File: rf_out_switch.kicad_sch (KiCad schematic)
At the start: 10 parts, among them P15 CONUFL001-SMD-T, P16 CONUFL001-SMD-T, U33 QPC1022TR7, U34 QPC1022TR7

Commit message: Work on cleaning up all values for things
Signed-off-by: Corey Minyard <corey@minyard.net>
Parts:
- R104, R109: value 50R >=2W -> 50Ω >=2W
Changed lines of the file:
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@@
 			)
 		)
-		(property "Value" "50R >=2W"
+		(property "Value" "50Ω >=2W"
 			(at 78.74 76.708 90)
 			(effects
@@
 			)
 		)
-		(property "Value" "50R >=2W"
+		(property "Value" "50Ω >=2W"
 			(at 195.834 110.998 90)
 			(effects

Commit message: Lots of updates to ease manufacturing
Component changes, changes in the formatting of the values, etc.

Signed-off-by: Corey Minyard <corey@minyard.net>
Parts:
- L39: value 470n -> 470nH
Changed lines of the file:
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@@
 			)
 		)
-		(property "Value" "470n"
+		(property "Value" "470nH"
 			(at 97.282 53.848 90)
 			(effects

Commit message: Update all resistors to have an ohm symbol
Make it more clean in the BOM what they are.

Signed-off-by: Corey Minyard <corey@minyard.net>
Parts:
- R105, R106: value 10K -> 10KΩ
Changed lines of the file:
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@@
 			)
 		)
-		(property "Value" "10K"
+		(property "Value" "10KΩ"
 			(at 86.868 140.843 0)
 			(effects
@@
 			)
 		)
-		(property "Value" "10K"
+		(property "Value" "10KΩ"
 			(at 86.868 130.683 0)
 			(effects

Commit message: Massive rework of filtering and inductors
Now that I know how inductors really work.

Signed-off-by: Corey Minyard <corey@minyard.net>
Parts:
- R107: now not fitted
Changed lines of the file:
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@@
 		(in_bom yes)
 		(on_board yes)
-		(dnp no)
+		(dnp yes)
 		(property "Reference" "R107"
 			(at 132.588 87.7316 0)

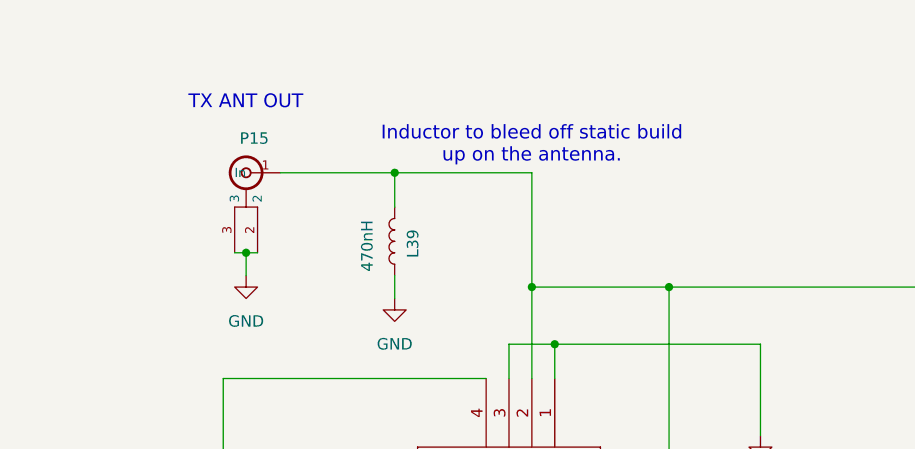
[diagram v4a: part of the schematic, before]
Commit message: More cleanups on the filtering
Signed-off-by: Corey Minyard <corey@minyard.net>
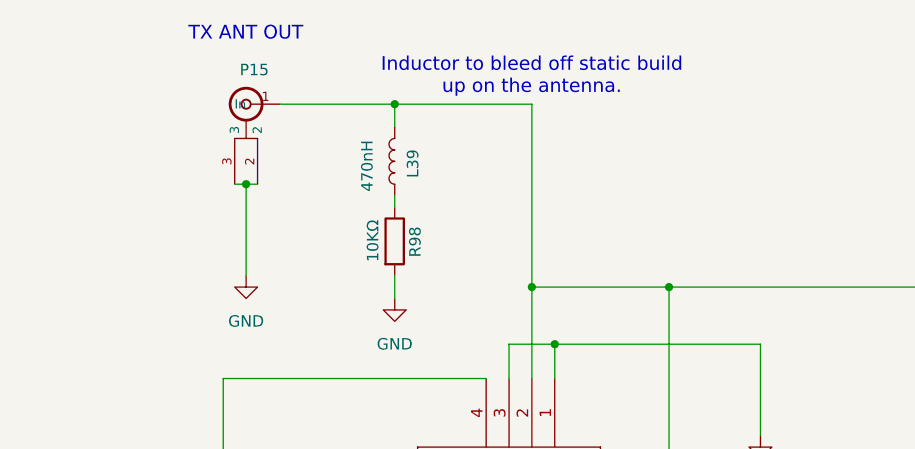
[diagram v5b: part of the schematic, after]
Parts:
- added R98: 10KΩ, Resistor_SMD:R_0402_1005Metric_Pad0.72x0.64mm_HandSolder, symbol Device:R
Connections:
- net GND: now also R98.2; no longer L39.2
- new net: L39.2, R98.1
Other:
- moved on the sheet: L39, P15
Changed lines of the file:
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@@
 	(text "TX ANT OUT"
 		(exclude_from_sim no)
-		(at 90.17 38.862 0)
+		(at 90.17 31.242 0)
 		(effects
 			(font
@@
 	(text "Inductor to bleed off static build\nup on the antenna."
 		(exclude_from_sim no)
-		(at 115.57 42.672 0)
+		(at 115.57 35.052 0)
 		(effects
 			(font
@@
 	)
 	(junction
-		(at 100.33 45.72)
-		(diameter 0)
-		(color 0 0 0 0)
-	)
-	(junction
-		(at 83.82 54.61)
+		(at 100.33 38.1)
 		(diameter 0)
 		(color 0 0 0 0)
@@
 	)
 	(junction
+		(at 83.82 46.99)
+		(diameter 0)
+		(color 0 0 0 0)
+	)
+	(junction
 		(at 115.57 58.42)
 		(diameter 0)
@@
 	(wire
 		(pts
-			(xy 100.33 45.72) (xy 115.57 45.72)
-		)
-		(stroke
-			(width 0)
-			(type default)
-		)
-	)
-	(wire
-		(pts
 			(xy 130.81 58.42) (xy 187.96 58.42)
 		)
@@
 	(wire
 		(pts
+			(xy 100.33 57.15) (xy 100.33 59.69)
+		)
+		(stroke
+			(width 0)
+			(type default)
+		)
+	)
+	(wire
+		(pts
 			(xy 172.72 46.99) (xy 172.72 49.53)
 		)
@@
 	(wire
 		(pts
-			(xy 87.63 45.72) (xy 100.33 45.72)
+			(xy 87.63 38.1) (xy 100.33 38.1)
 		)
 		(stroke
@@
 	(wire
 		(pts
-			(xy 83.82 54.61) (xy 85.09 54.61)
-		)
-		(stroke
-			(width 0)
-			(type default)
-		)
-	)
-	(wire
-		(pts
-			(xy 83.82 54.61) (xy 83.82 57.15)
+			(xy 100.33 48.26) (xy 100.33 49.53)
+		)
+		(stroke
+			(width 0)
+			(type default)
+		)
+	)
+	(wire
+		(pts
+			(xy 83.82 46.99) (xy 85.09 46.99)
+		)
+		(stroke
+			(width 0)
+			(type default)
+		)
+	)
+	(wire
+		(pts
+			(xy 83.82 46.99) (xy 83.82 57.15)
 		)
 		(stroke
@@
 	(wire
 		(pts
-			(xy 83.82 54.61) (xy 82.55 54.61)
+			(xy 83.82 46.99) (xy 82.55 46.99)
 		)
 		(stroke
@@
 	(wire
 		(pts
-			(xy 115.57 45.72) (xy 115.57 58.42)
+			(xy 115.57 38.1) (xy 115.57 58.42)
 		)
 		(stroke
@@
 	(wire
 		(pts
-			(xy 100.33 57.15) (xy 100.33 59.69)
-		)
-		(stroke
-			(width 0)
-			(type default)
-		)
-	)
-	(wire
-		(pts
 			(xy 81.28 68.58) (xy 110.49 68.58)
 		)
@@
 	(wire
 		(pts
+			(xy 100.33 38.1) (xy 115.57 38.1)
+		)
+		(stroke
+			(width 0)
+			(type default)
+		)
+	)
+	(wire
+		(pts
 			(xy 172.72 46.99) (xy 171.45 46.99)
 		)
@@
 	(wire
 		(pts
+			(xy 100.33 38.1) (xy 100.33 40.64)
+		)
+		(stroke
+			(width 0)
+			(type default)
+		)
+	)
+	(wire
+		(pts
 			(xy 190.5 99.06) (xy 190.5 118.11)
 		)
@@
 		(pts
 			(xy 193.04 125.73) (xy 207.01 125.73)
-		)
-		(stroke
-			(width 0)
-			(type default)
-		)
-	)
-	(wire
-		(pts
-			(xy 100.33 45.72) (xy 100.33 49.53)
 		)
 		(stroke
@@
 	(symbol
 		(lib_id "Device:L")
-		(at 100.33 53.34 0)
+		(at 100.33 44.45 0)
 		(mirror y)
 		(unit 1)
@@
 		(dnp no)
 		(property "Reference" "L39"
-			(at 102.362 53.594 90)
+			(at 102.362 44.704 90)
 			(effects
 				(font
@@
 		)
 		(property "Value" "470nH"
-			(at 97.282 53.848 90)
+			(at 97.282 44.958 90)
 			(effects
 				(font
@@
 		)
 		(property "Footprint" "Inductor_SMD:L_0805_2012Metric_Pad1.05x1.20mm_HandSolder"
-			(at 100.33 53.34 0)
+			(at 100.33 44.45 0)
 			(effects
 				(font
@@
 		)
 		(property "Datasheet" "~"
-			(at 100.33 53.34 0)
+			(at 100.33 44.45 0)
 			(effects
 				(font
@@
 		)
 		(property "Description" ""
-			(at 100.33 53.34 0)
+			(at 100.33 44.45 0)
 			(effects
 				(font
@@
 	)
 	(symbol
+		(lib_id "Device:R")
+		(at 100.33 53.34 0)
+		(unit 1)
+		(exclude_from_sim no)
+		(in_bom yes)
+		(on_board yes)
+		(dnp no)
+		(property "Reference" "R98"
+			(at 102.616 55.118 90)
+			(effects
+				(font
+					(size 1.27 1.27)
+				)
+				(justify left)
+			)
+		)
+		(property "Value" "10KΩ"
+			(at 97.917 55.626 90)
+			(effects
+				(font
+					(size 1.27 1.27)
+				)
+				(justify left)
+			)
+		)
+		(property "Footprint" "Resistor_SMD:R_0402_1005Metric_Pad0.72x0.64mm_HandSolder"
+			(at 98.552 53.34 90)
+			(effects
+				(font
+					(size 1.27 1.27)
+				)
+				(hide yes)
+			)
+		)
+		(property "Datasheet" "~"
+			(at 100.33 53.34 0)
+			(effects
+				(font
+					(size 1.27 1.27)
+				)
+			)
+		)
+		(property "Description" ""
+			(at 100.33 53.34 0)
+			(effects
+				(font
+					(size 1.27 1.27)
+				)
+			)
+		)
+		(pin "1"
+		)
+		(pin "2"
+		)
+		(instances
+			(project "PacSat_AFSK"
+				(path "/cc9f42d2-6985-41ac-acab-5ab7b01c5b38/4fa888af-703c-49ed-93bb-d56d2f02c470/26e0c845-9451-4c79-aef3-943c70af8ca9"
+					(reference "R98")
+					(unit 1)
+				)
+			)
+		)
+	)
+	(symbol
 		(lib_id "power:GND")
 		(at 207.01 72.39 0)
@@
 	(symbol
 		(lib_id "PACSAT_DEV_misc:U_FL")
-		(at 83.82 45.72 0)
+		(at 83.82 38.1 0)
 		(mirror y)
 		(unit 1)
@@
 		(dnp no)
 		(property "Reference" "P15"
-			(at 86.36 41.91 0)
+			(at 86.36 34.29 0)
 			(effects
 				(font
@@
 		)
 		(property "Value" "CONUFL001-SMD-T"
-			(at 83.82 45.72 0)
+			(at 83.82 38.1 0)
 			(effects
 				(font
@@
 		)
 		(property "Footprint" "PacSatDev_misc:CONN1_CONUFL_TEC"
-			(at 83.82 45.72 0)
+			(at 83.82 38.1 0)
 			(effects
 				(font
@@
 		)
 		(property "Datasheet" ""
-			(at 83.82 45.72 0)
+			(at 83.82 38.1 0)
 			(effects
 				(font
@@
 		)
 		(property "Description" ""
-			(at 83.82 45.72 0)
-			(effects
-				(font
+			(at 83.82 38.1 0)
+			(effects
+				(font

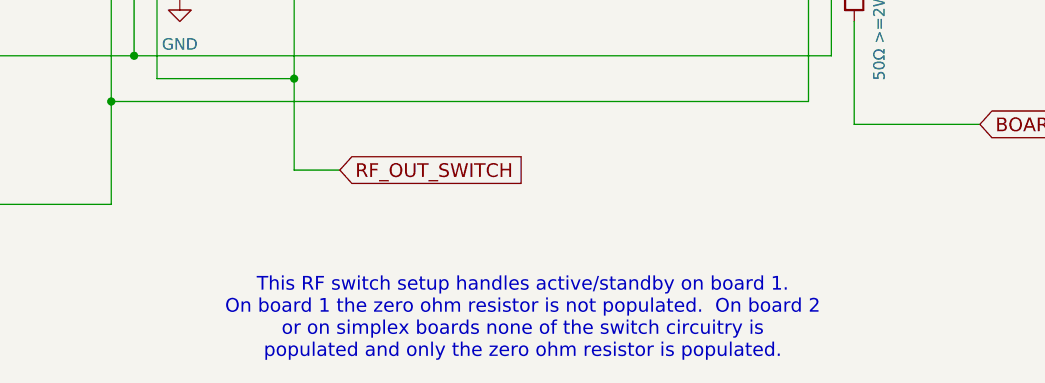
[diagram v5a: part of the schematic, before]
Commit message: Track and doc cleanups
Signed-off-by: Corey Minyard <corey@minyard.net>
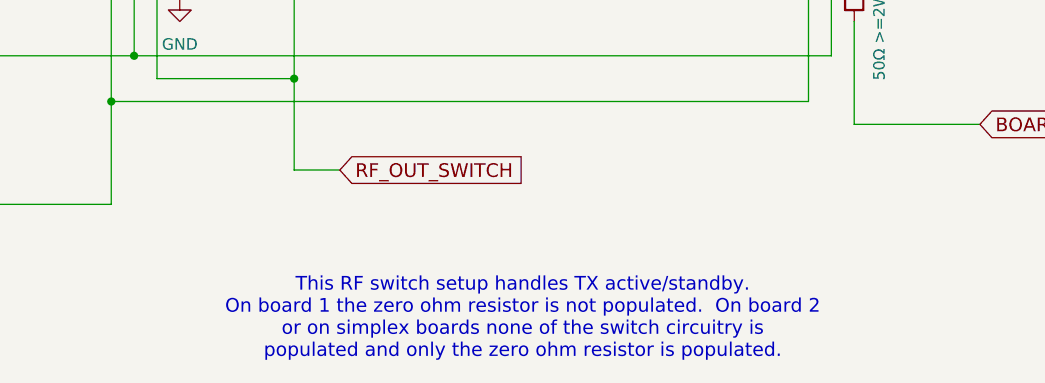
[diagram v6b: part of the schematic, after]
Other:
- note added: "This RF switch setup handles TX active/standby. On board 1 the zero ohm resistor is not populated. On board 2 or on simplex boards none of the switch circuitry is populated and only the zero ohm resistor is populated."
- note removed: "This RF switch setup handles active/standby on board 1. On board 1 the zero ohm resistor is not populated. On board 2 or on simplex boards none of the switch circuitry is populated and only the zero ohm resistor is populated."
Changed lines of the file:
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@@
 		)
 	)
-	(text "This RF switch setup handles active/standby on board 1.\nOn board 1 the zero ohm resistor is not populated.  On board 2\nor on simplex boards none of the switch circuitry is\npopulated and only the zero ohm resistor is populated."
+	(text "This RF switch setup handles TX active/standby.\nOn board 1 the zero ohm resistor is not populated.  On board 2\nor on simplex boards none of the switch circuitry is\npopulated and only the zero ohm resistor is populated."
 		(exclude_from_sim no)
 		(at 156.21 147.32 0)

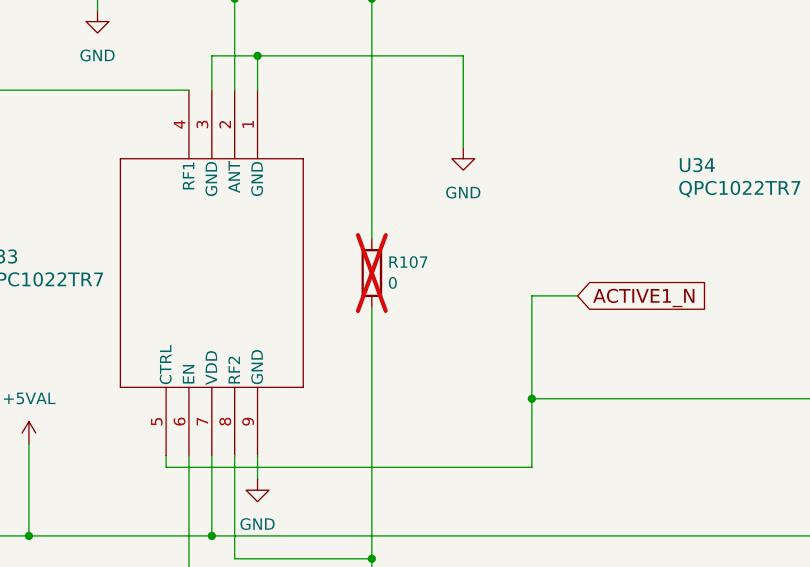
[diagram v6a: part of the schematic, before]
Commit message: Have the BOM file fixer output xls, not csv
The omega symbol gets translated properly from xls.

Signed-off-by: Corey Minyard <corey@minyard.net>
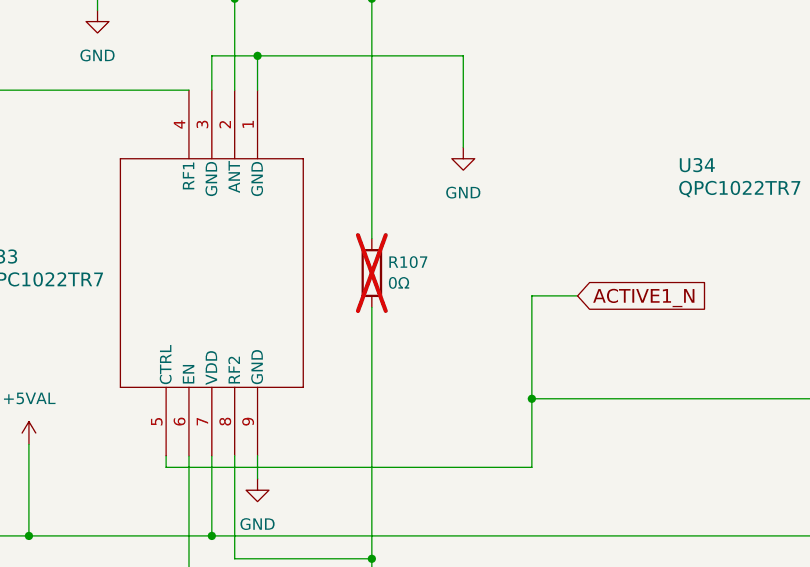
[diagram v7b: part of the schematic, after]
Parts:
- R107: value 0 -> 0Ω
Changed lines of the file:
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@@
 			)
 		)
-		(property "Value" "0"
+		(property "Value" "0Ω"
 			(at 132.588 90.043 0)
 			(effects

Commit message: Added some docs and notes about various things
Signed-off-by: Corey Minyard <corey@minyard.net>
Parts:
- R107: now left out of the parts list
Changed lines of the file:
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@@
 		(unit 1)
 		(exclude_from_sim no)
-		(in_bom yes)
+		(in_bom no)
 		(on_board yes)
 		(dnp yes)
